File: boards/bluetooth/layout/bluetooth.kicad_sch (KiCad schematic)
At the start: 9 parts, among them U1 HM-19

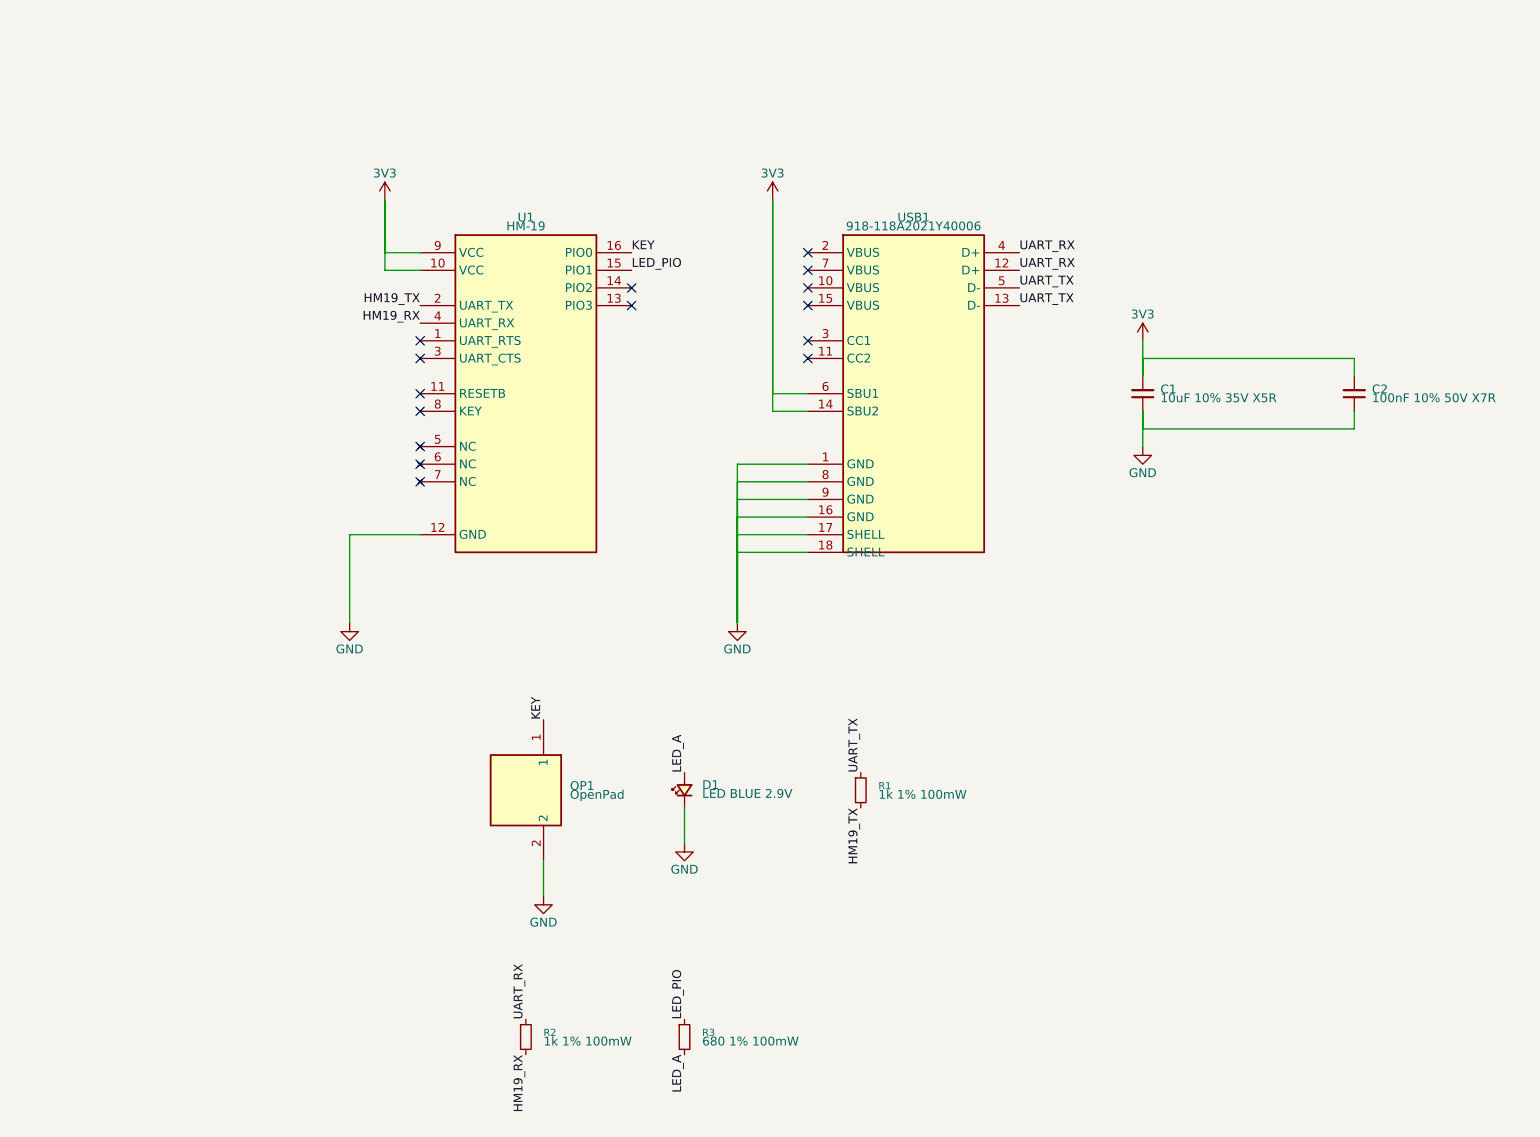
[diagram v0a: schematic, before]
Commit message: ✨ Place the schematics from per-sheet placement files
micras-pcb sch redraws each sheet pcb apply writes from
boards/<board>/schematic/<sheet>.toml: parts, wires, labels, power
symbols, titled frames, paper and title block, the root's sheet
symbols, and a ports column for the module sheets' extra labels. It
fails unless KiCad's netlist of the placed schematic equals pcb's.
make gen runs it after pcb apply; make check's sch gate fails on a part
without a placement, and tests/test_placement.py on any overlap.

The encoder and Bluetooth sheets are placed; the main board's DRIVERS
sheet is drafted.
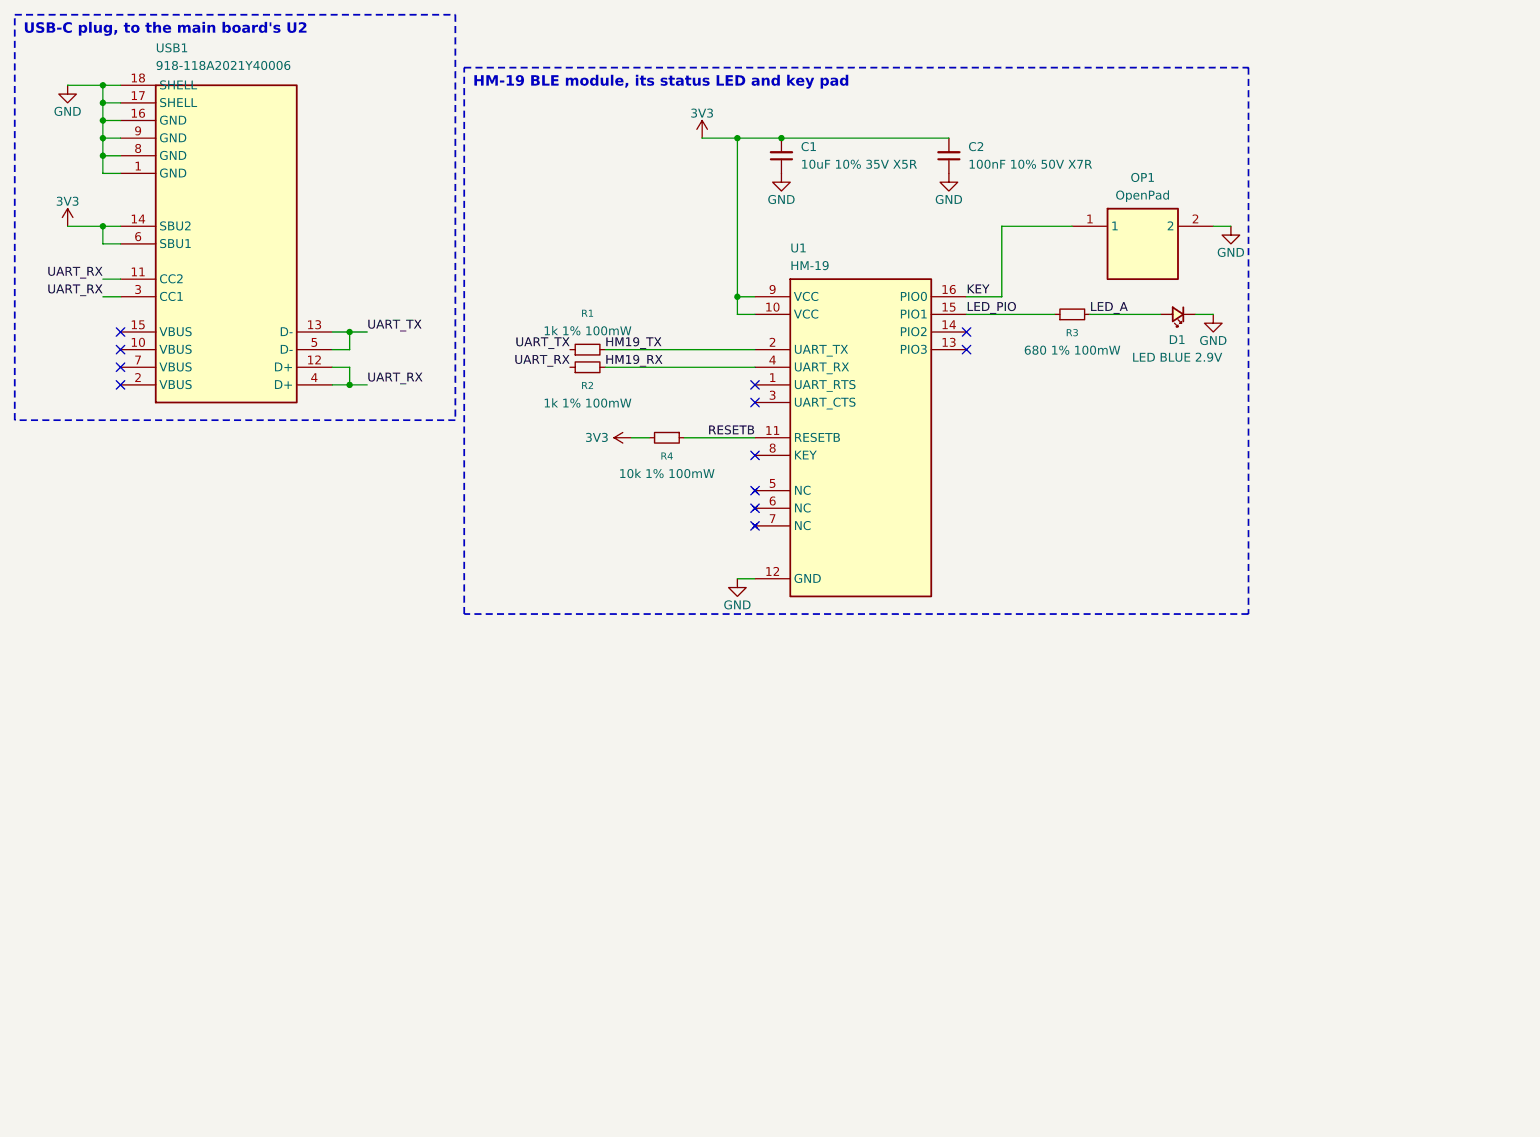
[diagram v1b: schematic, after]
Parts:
- added R4: 10k 1% 100mW, stdlib_kicad-footprints_Resistor_SMD:R_0603_1608Metric, symbol R_Small
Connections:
- net 3V3: now also R4.2
- net UART_RX: now also USB1.11 (CC2), USB1.3 (CC1)
- net RESETB: now reaches U1.11 (RESETB)
- net RESETB: now also R4.1
- no-connect marks 15 -> 12
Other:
- note added: "HM-19 BLE module, its status LED and key pad"
- note added: "USB-C plug, to the main board's U2"
- title: (none) -> Bluetooth module
- moved on the sheet: C1, C2, D1, OP1, R1, R2, R3, U1, USB1
